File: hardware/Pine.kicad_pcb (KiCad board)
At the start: 2 copper layers, 45.7 x 38.1 mm, 47 parts, among them J1 USB Micro type-B, J2 01x06 Male conn, J3 Battery connector, Q1 p-channel MOSFET, Q2 NPN Transistor, SW1 Switch, SW2 Push button, U1 IR Receiver, U2 LDO, U3 Temperature sensor, U4 MCU

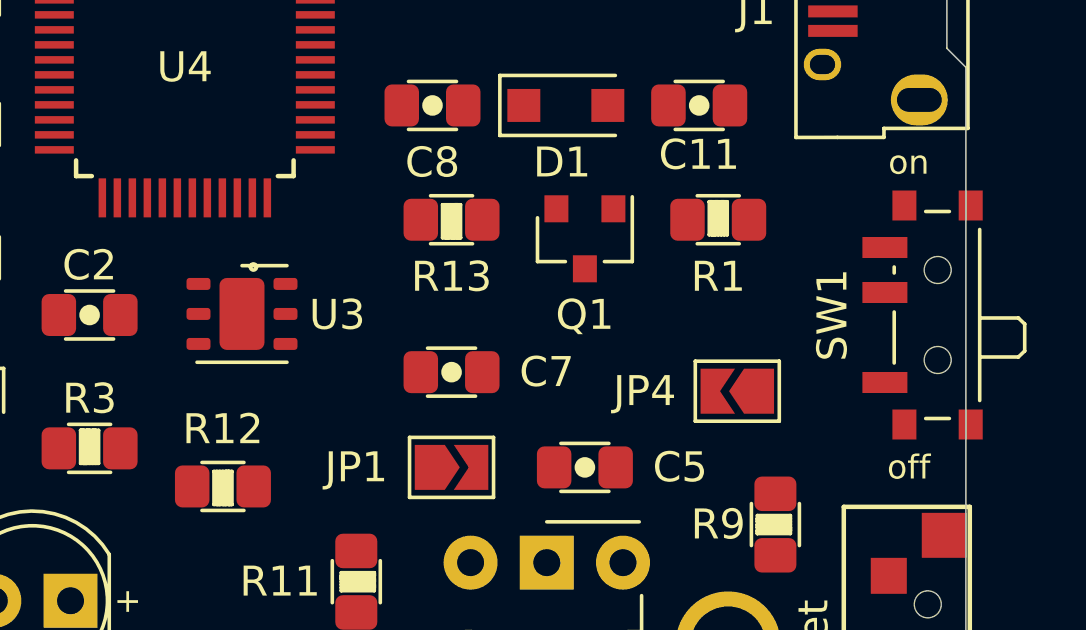
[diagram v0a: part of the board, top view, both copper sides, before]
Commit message: fix: use older breadboard schematic for getting started instructions
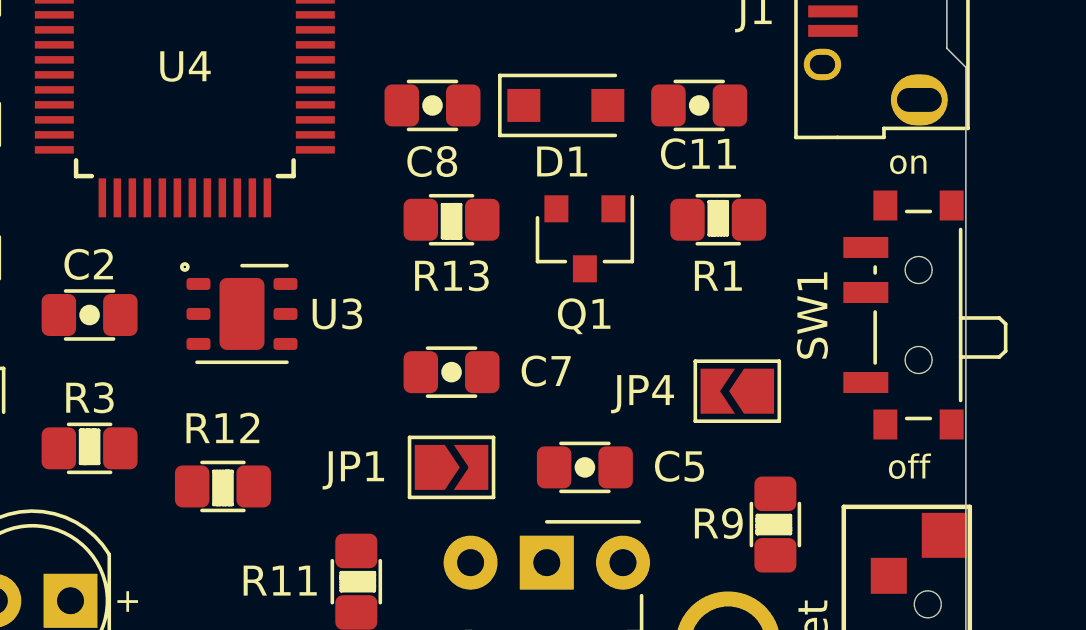
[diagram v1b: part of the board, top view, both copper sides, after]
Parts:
- moved SW1 0.64 mm to (196.8, 62.2)
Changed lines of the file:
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@@
   )
   (layers
-    (0 F.Cu signal hide)
-    (31 B.Cu signal)
+    (0 F.Cu signal)
+    (31 B.Cu signal hide)
     (32 B.Adhes user hide)
     (33 F.Adhes user hide)
-    (34 B.Paste user)
-    (35 F.Paste user hide)
-    (36 B.SilkS user)
-    (37 F.SilkS user hide)
-    (38 B.Mask user)
-    (39 F.Mask user hide)
+    (34 B.Paste user hide)
+    (35 F.Paste user)
+    (36 B.SilkS user hide)
+    (37 F.SilkS user)
+    (38 B.Mask user hide)
+    (39 F.Mask user)
     (40 Dwgs.User user hide)
     (41 Cmts.User user hide)
@@
     (44 Edge.Cuts user)
     (45 Margin user hide)
-    (46 B.CrtYd user)
-    (47 F.CrtYd user hide)
+    (46 B.CrtYd user hide)
+    (47 F.CrtYd user)
     (48 B.Fab user hide)
     (49 F.Fab user hide)
@@
     (solder_mask_min_width 0.25)
     (aux_axis_origin 0 0)
-    (visible_elements FFFFE77F)
+    (visible_elements FFFFFF7F)
     (pcbplotparams
       (layerselection 0x010fc_ffffffff)
@@
   )
   (module Button_Switch_SMD:SW_SPDT_PCM12 (layer F.Cu)
-    (at 197.485 62.23 90)
+    (at 196.85 62.23 90)
     (descr "Ultraminiature Surface Mount Slide Switch")
     (attr smd)
@@
   )
   (gr_line (start 153.035 44.45) (end 153.035 77.47) (layer Edge.Cuts) (width 0.05))
-  (gr_circle (center 175.006 60.6298) (end 174.9044 60.6298) (layer F.SilkS) (width 0.12))
+  (gr_circle (center 172.72 60.6298) (end 172.6184 60.6298) (layer F.SilkS) (width 0.12))
   (gr_line (start 154.305 45.085) (end 154.305 46.355) (layer F.SilkS) (width 0.12))
   (gr_line (start 158.115 45.085) (end 154.305 45.085) (layer F.SilkS) (width 0.12))

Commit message: feat: continue with routing
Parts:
- removed REF**: OSHW-Logo2_9.8x8mm_SilkScreen, Symbol:OSHW-Logo2_9.8x8mm_SilkScreen
- moved C4 5.18 mm to (177.5, 43.9)
- moved C10 1.27 mm to (184.8, 47.6)
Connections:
- D4 pad 1: (no net) -> Net-(D4-Pad1)
- D4 pad 2: (no net) -> /2V8
- D5 pad 1: (no net) -> Net-(D5-Pad1)
- D5 pad 2: (no net) -> /2V8
- D6 pad 1: (no net) -> Net-(D6-Pad1)
- D6 pad 2: (no net) -> /2V8
- D7 pad 1: (no net) -> Net-(D7-Pad1)
- D7 pad 2: (no net) -> /2V8
- R10 pad 1: (no net) -> Net-(D7-Pad1)
- R6 pad 1: (no net) -> Net-(D4-Pad1)
- R7 pad 1: (no net) -> Net-(D5-Pad1)
- R8 pad 1: (no net) -> Net-(D6-Pad1)
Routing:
- net Net-(D2-Pad1): track 0.00 -> 51.5 mm, vias 0 -> 2
- net GND: track 0.00 -> 50.2 mm, vias 0 -> 20
- net Net-(C7-Pad1): track 0.00 -> 29.6 mm
- net /RST: track 0.00 -> 28.8 mm
- net /LED: track 0.00 -> 21.3 mm
- net Net-(C11-Pad1): track 0.00 -> 18.9 mm
- net /USB_D+: track 0.00 -> 17.6 mm
- net Net-(J1-Pad6): track 0.00 -> 17.5 mm
- net /USB_D-: track 0.00 -> 17.5 mm
- net /2V8: track 0.00 -> 17.3 mm
- net /TX_LED: track 0.00 -> 15.5 mm
- net /Batt_EN: track 0.00 -> 14.2 mm
- net Net-(C5-Pad1): track 0.00 -> 12.9 mm
- net /SWD_POWER_IN: track 0.00 -> 10.8 mm
- net /VBAT: track 0.00 -> 10.7 mm
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- added copper zone on F.Cu, net /2V8
- added copper zone on B.Cu, net GND

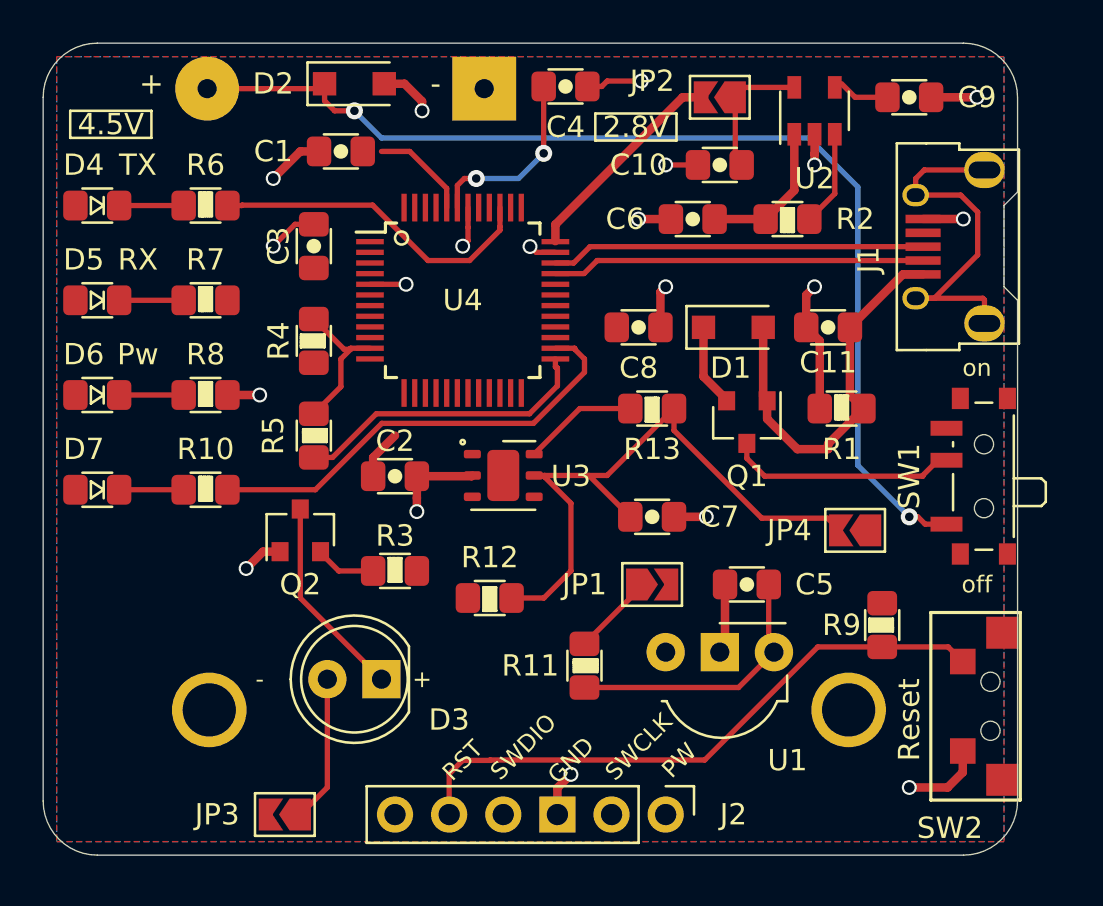
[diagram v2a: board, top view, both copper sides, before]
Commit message: feat: add 4 test points in schematic and layout. close #6
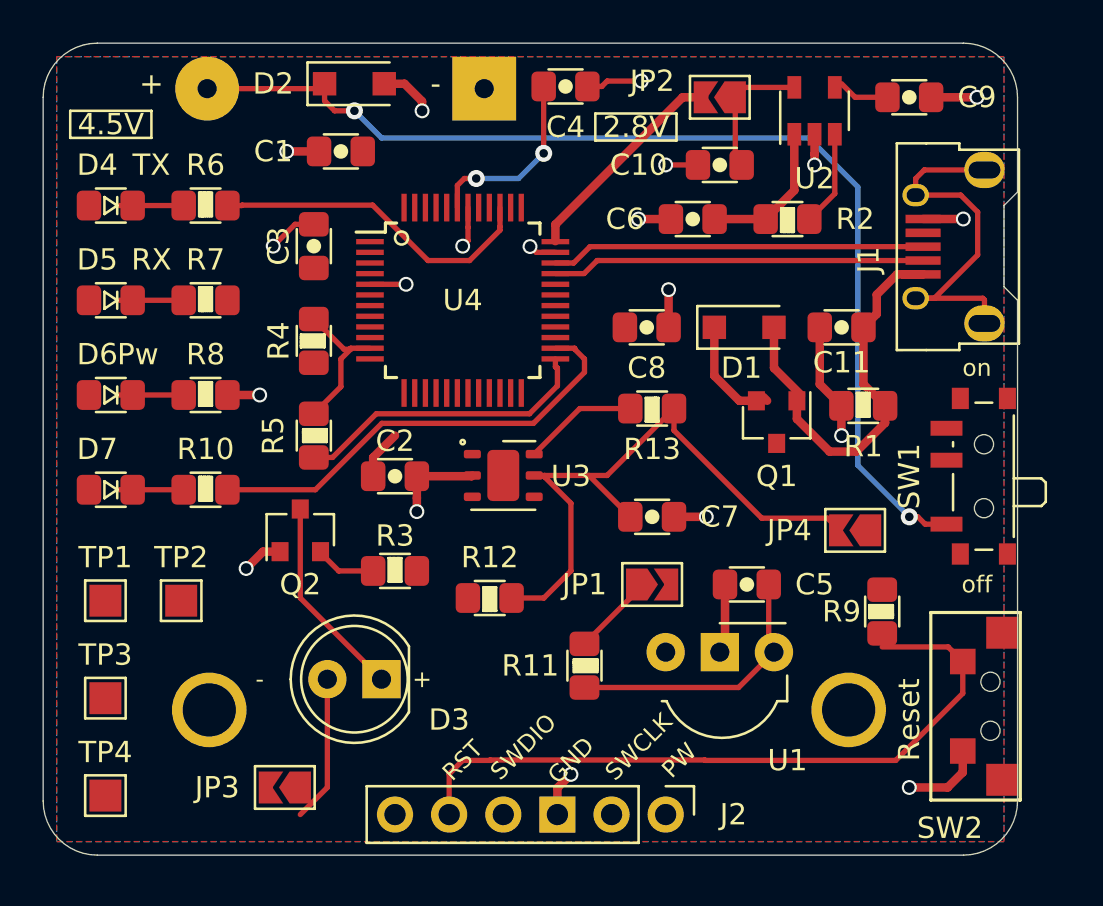
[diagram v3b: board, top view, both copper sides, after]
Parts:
- added TP1: TestPoint_Probe, TestPoint:TestPoint_Pad_1.5x1.5mm, F.Cu at (156.0, 68.1)
- added TP2: TestPoint_Probe, TestPoint:TestPoint_Pad_1.5x1.5mm, F.Cu at (159.5, 68.1)
- added TP3: TestPoint_Probe, TestPoint:TestPoint_Pad_1.5x1.5mm, F.Cu at (156.0, 72.6)
- added TP4: TestPoint_Probe, TestPoint:TestPoint_Pad_1.5x1.5mm, F.Cu at (156.0, 77.2)
- moved Q1 1.40 mm to (187.5, 59.7)
- moved JP3 1.27 mm to (164.4, 76.8)
- moved R1 1.02 mm to (191.5, 58.9)
- moved D4 0.64 mm to (156.2, 49.5)
- moved D5 0.64 mm to (156.2, 54.0)
- moved D6 0.64 mm to (156.2, 58.4)
- moved D7 0.64 mm to (156.2, 62.9)
- moved R9 0.64 mm to (192.4, 68.6)
- moved C11 0.63 mm to (190.5, 55.2)
- moved D1 0.51 mm to (185.9, 55.2)
- moved C8 0.38 mm to (181.4, 55.2)
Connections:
- U4 pad 21: (no net) -> Net-(TP3-Pad1)
- U4 pad 22: (no net) -> Net-(TP4-Pad1)
- U4 pad 7: (no net) -> Net-(TP1-Pad1)
- U4 pad 8: (no net) -> Net-(TP2-Pad1)
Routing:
- net /VBAT: track 10.7 -> 0.40 mm
- net /2V8: track 17.3 -> 12.6 mm
- net /RST: track 28.8 -> 33.1 mm
- net GND: track 50.2 -> 48.2 mm
- net Net-(C11-Pad1): track 18.9 -> 20.1 mm
- net /SWD_POWER_IN: track 10.8 -> 11.9 mm

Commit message: feat: complete first cut routing with DRC passing
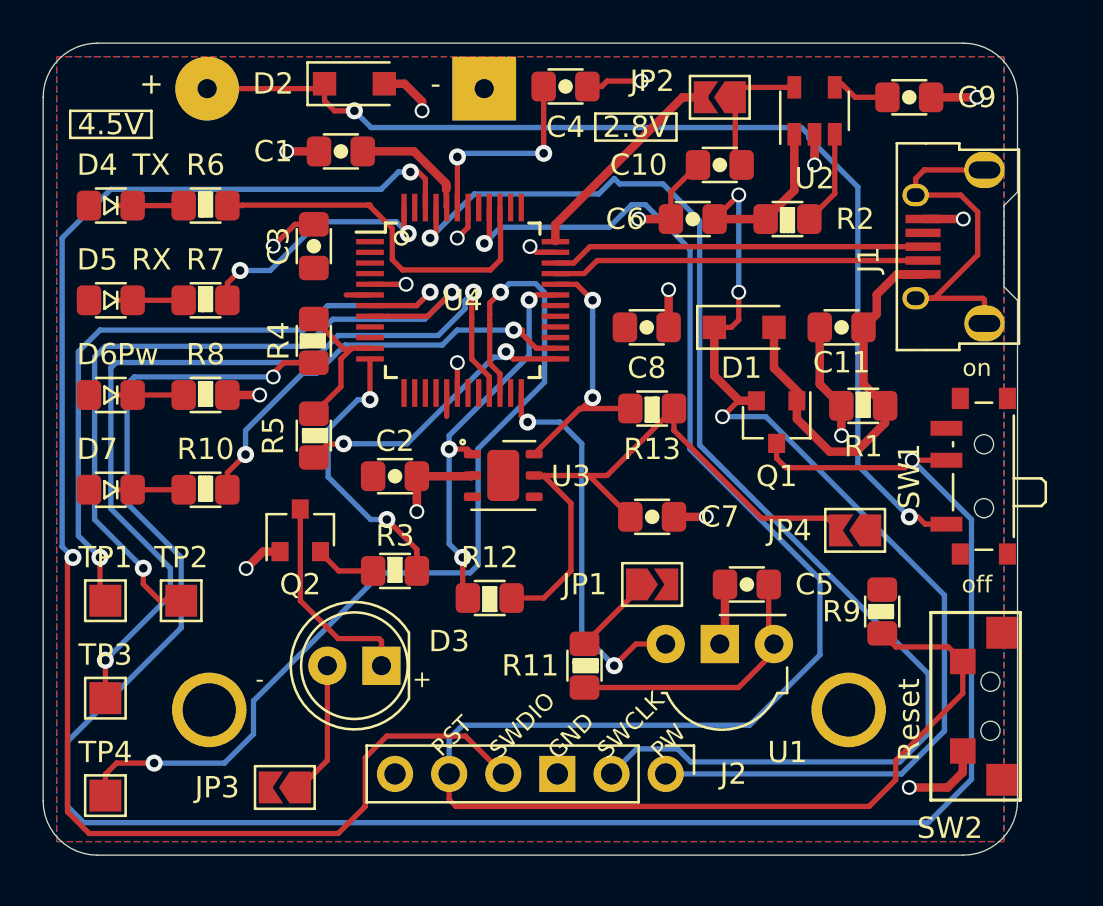
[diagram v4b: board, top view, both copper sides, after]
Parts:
- moved J2 1.91 mm to (182.2, 76.2)
- moved D3 0.63 mm to (168.9, 71.1)
- moved U1 0.38 mm to (182.2, 70.1)
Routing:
- net /VBAT: track 0.40 -> 101.4 mm, vias 0 -> 2
- net /SWDIO: track 0.00 -> 72.1 mm, vias 0 -> 2
- net /SWCLK: track 0.00 -> 60.8 mm, vias 0 -> 1
- net /RST: track 33.1 -> 89.3 mm, vias 0 -> 1
- net Net-(TP4-Pad1): track 0.00 -> 45.1 mm, vias 0 -> 2
- net /SWD_POWER_IN: track 11.9 -> 55.7 mm, vias 0 -> 3
- net Net-(TP3-Pad1): track 0.00 -> 41.7 mm, vias 0 -> 2
- net Net-(TP2-Pad1): track 0.00 -> 36.0 mm, vias 0 -> 2
- net Net-(TP1-Pad1): track 0.00 -> 33.0 mm, vias 0 -> 2
- net /SDA: track 0.00 -> 18.4 mm, vias 0 -> 3
- net /IR_Receiver: track 0.00 -> 18.3 mm, vias 0 -> 2
- net /IR_Emitter: track 0.00 -> 13.3 mm, vias 0 -> 2
- net /RX_LED: track 0.00 -> 12.0 mm, vias 0 -> 2
- net /SCL: track 5.40 -> 12.8 mm, vias 0 -> 2
- net /2V8: track 12.6 -> 18.3 mm
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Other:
- net class Power_thin added: clearance 0.2, trace_width 0.25, via_dia 0.8, via_drill 0.4

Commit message: feat: improve routing
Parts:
- added REF**: OSHW-Logo2_9.8x8mm_SilkScreen, Symbol:OSHW-Logo2_9.8x8mm_SilkScreen, B.Cu at (176.0, 58.9)
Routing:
- net /SWCLK: track 60.8 -> 63.0 mm
- net /RST: track 89.3 -> 90.5 mm
- net /SWD_POWER_IN: track 55.7 -> 55.2 mm
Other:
- board text added: "CLK"
- board text added: "DIO"
- board text removed: "SWCLK"
- board text removed: "SWDIO"
